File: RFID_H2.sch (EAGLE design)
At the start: 11 parts, among them IC1 RASPBERRY_PI_ZERO_W__V1.3_, M1 ARDUINO-NANO-3.0, X2 JST-XH-06-PIN-ROUND-PAD

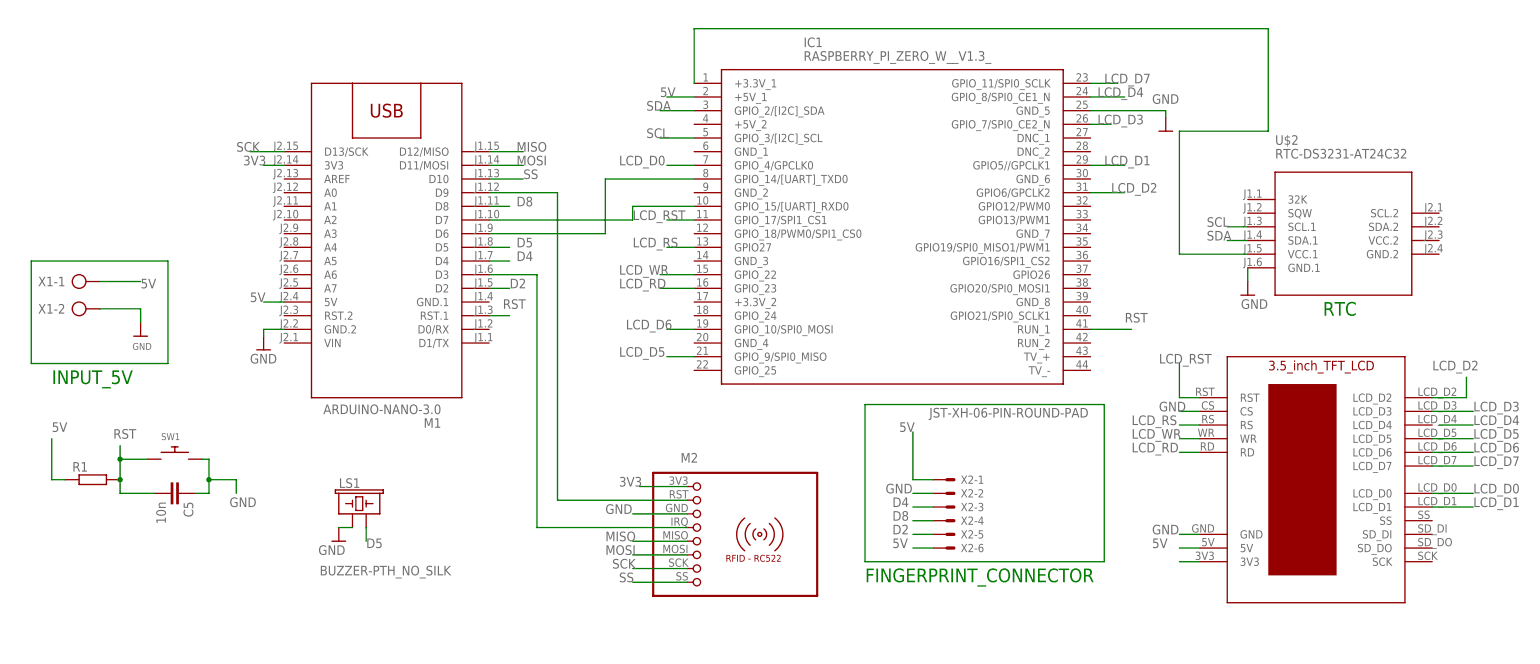
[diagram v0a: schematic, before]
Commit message: Whole circuit on 3.3V logic level and no level shifter needed
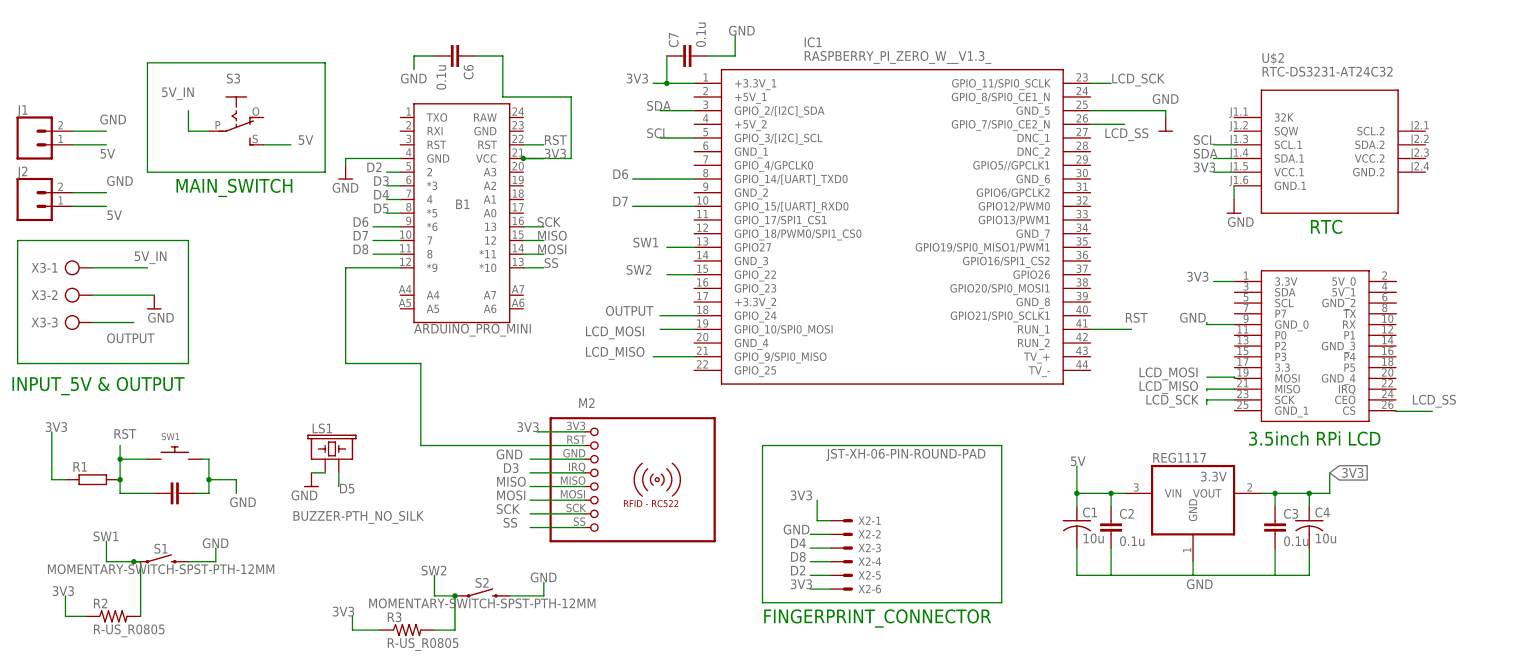
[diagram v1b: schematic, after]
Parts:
- removed M1: ARDUINO-NANO-3.0, diy-modules:ARDUINO-NANO-3.0
- removed X1: (no value), con-ptr500:AK500/2-H
- added B1: ARDUINO_PRO_MINI, SparkFun-Boards:ARDUINO_PRO_MINI
- added C1, C4: 10u, rcl:C-USC0805
- added C2, C3, C6, C7: 0.1u, rcl:C-EUC0805
- added J1, J2: (no value), SparkFun-Connectors:CONN_02
- added R2, R3: R-US_R0805, audio amplifier example:R-US_R0805
- added REG1117: 3.3V, burr-brown:REG1117
- added S1, S2: MOMENTARY-SWITCH-SPST-PTH-12MM, SparkFun-Switches:MOMENTARY-SWITCH-SPST-PTH-12MM
- added S3: (no value), adafruit:EG1218S
- added X3: (no value), con-ptr500:AK500/3-H
- U$7: value 3.5_INCH_TFT_LCD -> 3.5_INCH_TOUCHSCREEN; device 3.5_inch_tft_lcd:3.5_INCH_TFT_LCD -> 3.5_inch_touchscreen:3.5_INCH_TOUCHSCREEN
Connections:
- removed net LCD_D0: IC1.GPIO_4/GPCLK0, U$7.LCD_D0
- removed net LCD_D1: IC1.GPIO5//GPCLK1, U$7.LCD_D1
- removed net LCD_D2: IC1.GPIO6/GPCLK2, U$7.LCD_D2
- removed net LCD_D3: IC1.GPIO_7/SPI0_CE2_N, U$7.LCD_D3
- removed net LCD_D4: IC1.GPIO_8/SPI0_CE1_N
- removed net LCD_D5: IC1.GPIO_9/SPI0_MISO, U$7.LCD_D5
- removed net LCD_D6: IC1.GPIO_10/SPI0_MOSI, U$7.LCD_D6
- removed net LCD_D7: IC1.GPIO_11/SPI0_SCLK, U$7.LCD_D7
- removed net LCD_RD: IC1.GPIO_23, U$7.RD
- removed net LCD_RS: IC1.GPIO27, U$7.RS
- removed net LCD_RST: IC1.GPIO_17/SPI1_CS1, U$7.RST
- removed net LCD_WR: IC1.GPIO_22, U$7.WR
- removed net N$10: U$7.3V3
- removed net N$2: M1.D3, M2.4
- removed net N$3: IC1.GPIO_14/[UART]_TXD0, M1.D6
- removed net N$4: IC1.GPIO_15/[UART]_RXD0, M1.D7
- removed net N$5: IC1.+3.3V_1, U$2.VCC.1
- new net 5V_IN: S3.P, X3-1.KL
- new net D3: B1.*3, M2.4
- new net D6: B1.*6, IC1.GPIO_14/[UART]_TXD0
- new net D7: B1.7, IC1.GPIO_15/[UART]_RXD0
- new net LCD_MISO: IC1.GPIO_9/SPI0_MISO, U$7.MISO
- new net LCD_MOSI: IC1.GPIO_10/SPI0_MOSI, U$7.MOSI
- new net LCD_SCK: IC1.GPIO_11/SPI0_SCLK, U$7.SCK
- new net LCD_SS: IC1.GPIO_7/SPI0_CE2_N, U$7.CS
- new net OUTPUT: IC1.GPIO_24, X3-3.KL
- new net SW1: IC1.GPIO27, R2.2, S1.1
- new net SW2: IC1.GPIO_22, R3.2, S2.1
- net 3V3: now also B1.VCC, C3.1, C4.1, C6.1, C7.1, IC1.+3.3V_1, R1.1, R2.1, R3.1, REG1117.VOUT, U$2.VCC.1, U$7.3.3V, X2-1.S, X2-6.S; no longer M1.3V3
- net 5V: now also C1.1, C2.1, J1.1, J2.1, REG1117.VIN, S3.S; no longer IC1.+5V_1, M1.5V, R1.1, U$7.5V, X1-1.KL, X2-1.S, X2-6.S
- net D2: now also B1.2; no longer M1.D2
- net D4: now also B1.4; no longer M1.D4
- net D5: now also B1.*5; no longer M1.D5
- net D8: now also B1.8; no longer M1.D8
- net GND: now also B1.GND, C1.2, C2.2, C3.2, C4.2, C6.2, C7.2, J1.2, J2.2, REG1117.GND, S1.2, S2.2, U$7.GND_0, X3-2.KL; no longer M1.GND.2, U$7.CS, U$7.GND, X1-2.KL
- net MISO: now also B1.12; no longer M1.D12/MISO
- net MOSI: now also B1.*11; no longer M1.D11/MOSI
- net N$1: now also B1.*9; no longer M1.D9
- net RST: now also B1.RST@2; no longer M1.RST.1
- net SCK: now also B1.13; no longer M1.D13/SCK
- net SS: now also B1.*10; no longer M1.D10
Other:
- note added: "3.5inch RPi LCD"
- note added: "INPUT_5V & OUTPUT"
- note added: "MAIN_SWITCH"
- note removed: "INPUT_5V"
- moved on the sheet: LS1, M2, U$2, X2-1, X2-2, X2-3, X2-4, X2-5, X2-6
